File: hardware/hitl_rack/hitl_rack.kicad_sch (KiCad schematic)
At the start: 14 parts, among them J1 KH-1.27PH180-2X5P-L7.2-SMT, SW1 TS-1187A-B-A-B, U1 BlackPill

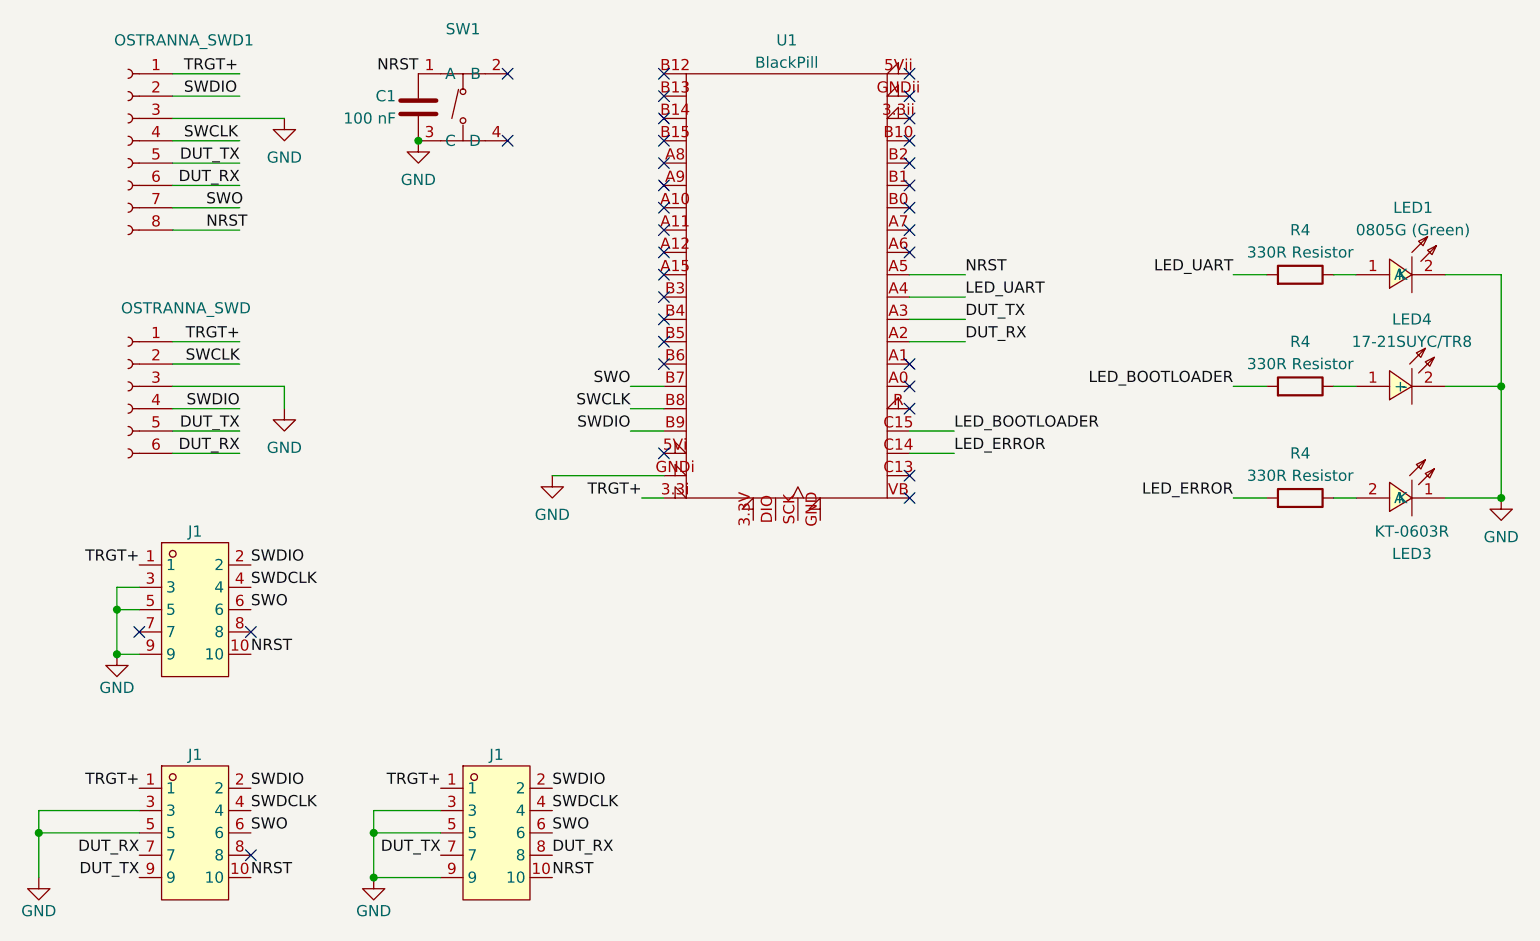
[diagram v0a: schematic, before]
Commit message: Finalize HITL rack PCB design and send to production
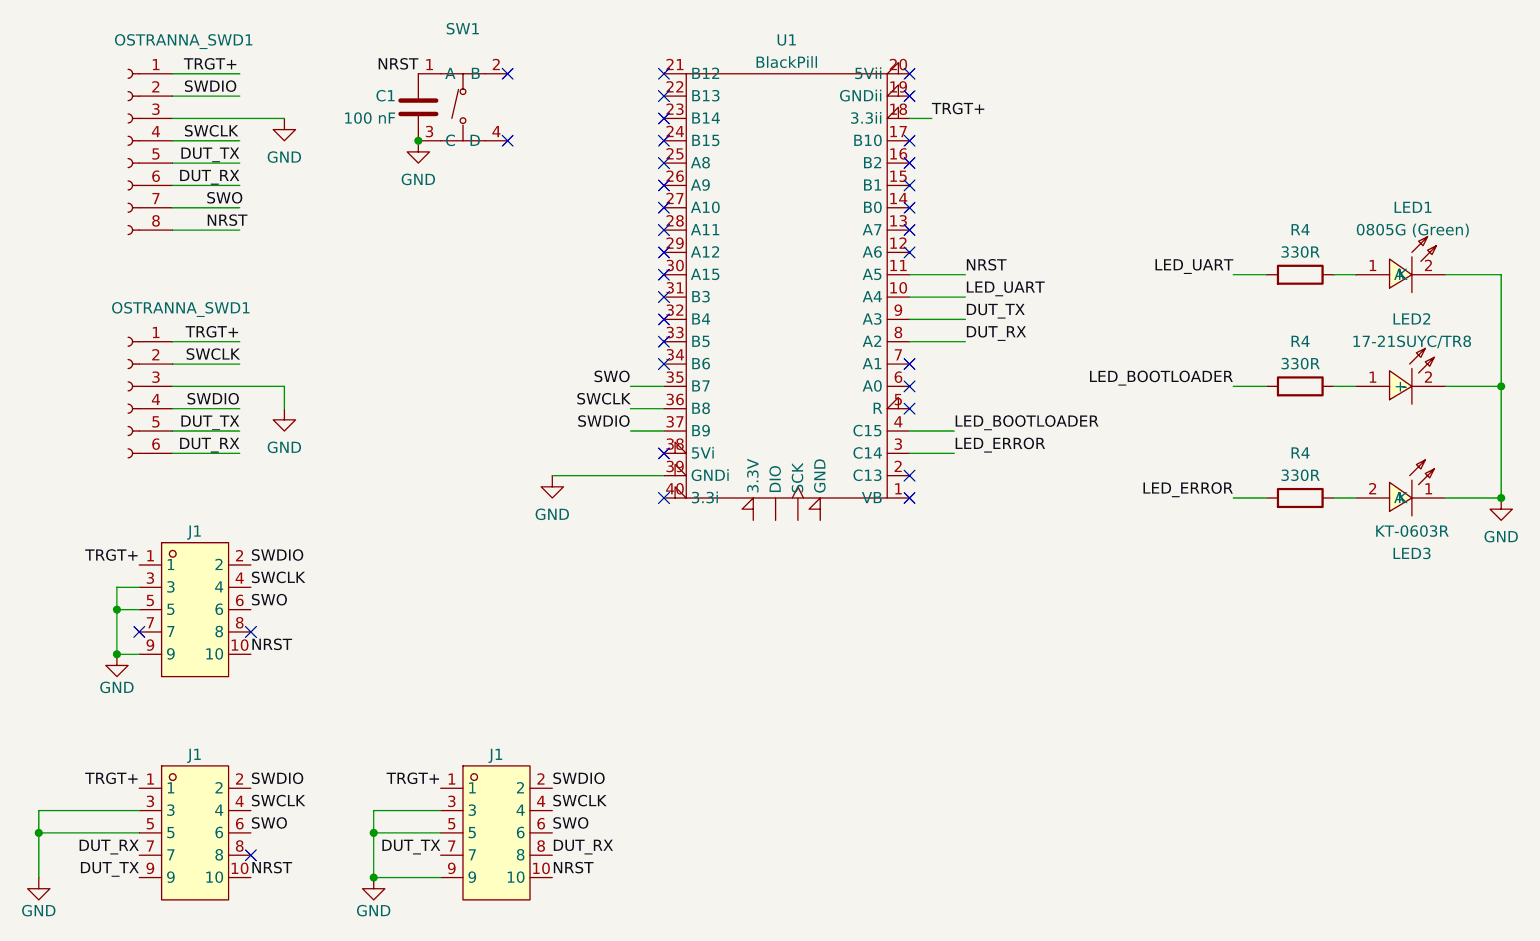
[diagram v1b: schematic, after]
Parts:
- R4: value 330R Resistor -> 330R
- renumbered LED4 to LED2, OSTRANNA_SWD to OSTRANNA_SWD1
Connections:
- net SWDCLK is gone; now on net SWCLK: J1.4, J1.4, J1.4
- net DUT_RX: now also U1.8 (A2); no longer U1.A2
- net DUT_TX: now also U1.9 (A3); no longer U1.A3
- net GND: now also U1.39 (GNDi); no longer U1.GNDi
- net LED_BOOTLOADER: now also U1.4 (C15); no longer U1.C15
- net LED_ERROR: now also U1.3 (C14); no longer U1.C14
- net LED_UART: now also U1.10 (A4); no longer U1.A4
- net NRST: now also U1.11 (A5); no longer U1.A5
- net SWCLK: now also U1.36 (B8); no longer U1.B8
- net SWDIO: now also U1.37 (B9); no longer U1.B9
- net SWO: now also U1.35 (B7); no longer U1.B7
- net TRGT+: now also U1.18 (3.3ii); no longer U1.3.3i
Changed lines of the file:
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@@
   (no_connect (at 121.92 101.6))
   (no_connect (at 149.86 83.82))
+  (no_connect (at 121.92 124.46))
   (no_connect (at 121.92 119.38))
   (no_connect (at 121.92 83.82))
@@
   (no_connect (at 121.92 106.68))
   (no_connect (at 149.86 88.9))
-  (no_connect (at 149.86 81.28))
   (no_connect (at 74.93 165.1))
   (no_connect (at 121.92 96.52))
@@
     (stroke (width 0) (type default))
   )
-  (wire (pts (xy 119.38 124.46) (xy 121.92 124.46))
-    (stroke (width 0) (type default))
-  )
   (wire (pts (xy 66.04 86.36) (xy 73.66 86.36))
     (stroke (width 0) (type default))
@@
     (stroke (width 0) (type default))
   )
+  (wire (pts (xy 152.4 81.28) (xy 149.86 81.28))
+    (stroke (width 0) (type default))
+  )
   (wire (pts (xy 198.12 111.76) (xy 200.66 111.76))
     (stroke (width 0) (type default))
@@
     (stroke (width 0) (type default))
   )
-  (label "SWDCLK" (at 74.93 160.02 0) (fields_autoplaced)
+  (label "SWCLK" (at 74.93 160.02 0) (fields_autoplaced)
     (effects (font (size 1.27 1.27)) (justify left bottom))
   )
@@
     (effects (font (size 1.27 1.27)) (justify right bottom))
   )
+  (label "TRGT+" (at 152.4 81.28 0) (fields_autoplaced)
+    (effects (font (size 1.27 1.27)) (justify left bottom))
+  )
   (label "LED_UART" (at 156.21 101.6 0) (fields_autoplaced)
     (effects (font (size 1.27 1.27)) (justify left bottom))
@@
     (effects (font (size 1.27 1.27)) (justify right bottom))
   )
-  (label "SWDCLK" (at 74.93 134.62 0) (fields_autoplaced)
-    (effects (font (size 1.27 1.27)) (justify left bottom))
-  )
-  (label "SWDCLK" (at 109.22 160.02 0) (fields_autoplaced)
+  (label "SWCLK" (at 74.93 134.62 0) (fields_autoplaced)
+    (effects (font (size 1.27 1.27)) (justify left bottom))
+  )
+  (label "SWCLK" (at 109.22 160.02 0) (fields_autoplaced)
     (effects (font (size 1.27 1.27)) (justify left bottom))
   )
@@
   )
   (label "DUT_TX" (at 96.52 165.1 180) (fields_autoplaced)
-    (effects (font (size 1.27 1.27)) (justify right bottom))
-  )
-  (label "TRGT+" (at 119.38 124.46 180) (fields_autoplaced)
     (effects (font (size 1.27 1.27)) (justify right bottom))
   )
@@
       (effects (font (size 1.27 1.27)))
     )
-    (property "Value" "330R Resistor" (at 194.31 121.92 90)
+    (property "Value" "330R" (at 194.31 121.92 90)
       (effects (font (size 1.27 1.27)))
     )
@@
   (symbol (lib_id "easyeda2kicad:17-21SUYC_TR8") (at 205.74 111.76 0) (mirror y) (unit 1)
     (in_bom yes) (on_board yes) (dnp no) (fields_autoplaced)
-    (property "Reference" "LED4" (at 207.01 104.14 0)
+    (property "Reference" "LED2" (at 207.01 104.14 0)
       (effects (font (size 1.27 1.27)))
     )
@@
       (project "hitl_rack"
         (path "/f0c86ddf-9c86-49a8-ba85-db01cb1dc88e"
-          (reference "LED4") (unit 1)
+          (reference "LED2") (unit 1)
         )
       )
@@
       (project "hitl_rack"
         (path "/f0c86ddf-9c86-49a8-ba85-db01cb1dc88e"
-          (reference "MANUAL_RESET") (unit 1)
+          (reference "MANUAL_RESET1") (unit 1)
         )
       )
@@
       (effects (font (size 1.27 1.27)))
     )
-    (property "Value" "330R Resistor" (at 194.31 96.52 90)
+    (property "Value" "330R" (at 194.31 96.52 90)
       (effects (font (size 1.27 1.27)))
     )
@@
       (project "hitl_rack"
         (path "/f0c86ddf-9c86-49a8-ba85-db01cb1dc88e"
-          (reference "ARM_CORTEX_CANONICAL") (unit 1)
+          (reference "ARM_CORTEX_CANONICAL1") (unit 1)
         )
       )
@@
       (effects (font (size 1.27 1.27)))
     )
-    (property "Value" "330R Resistor" (at 194.31 109.22 90)
+    (property "Value" "330R" (at 194.31 109.22 90)
       (effects (font (size 1.27 1.27)))
     )
@@
       (project "hitl_rack"
         (path "/f0c86ddf-9c86-49a8-ba85-db01cb1dc88e"
-          (reference "BLACK_MAGIC_UNIFIED") (unit 1)
+          (reference "BLACK_MAGIC_UNIFIED1") (unit 1)
         )
       )
@@
   (symbol (lib_id "Connector:Conn_01x06_Socket") (at 60.96 111.76 0) (mirror y) (unit 1)
     (in_bom yes) (on_board yes) (dnp no)
-    (property "Reference" "OSTRANNA_SWD" (at 74.93 102.87 0)
+    (property "Reference" "OSTRANNA_SWD1" (at 74.93 102.87 0)
       (effects (font (size 1.27 1.27)) (justify left))
     )
@@
       (project "hitl_rack"
         (path "/f0c86ddf-9c86-49a8-ba85-db01cb1dc88e"
-          (reference "OSTRANNA_SWD") (unit 1)
+          (reference "OSTRANNA_SWD1") (unit 1)
         )
       )
@@
       (project "hitl_rack"
         (path "/f0c86ddf-9c86-49a8-ba85-db01cb1dc88e"
-          (reference "ARM_CORTEX_EXTENDED") (unit 1)
+          (reference "ARM_CORTEX_EXTENDED1") (unit 1)
         )
       )
@@
       (project "hitl_rack"
         (path "/f0c86ddf-9c86-49a8-ba85-db01cb1dc88e"
-          (reference "FIREFLY_SWD") (unit 1)
+          (reference "FIREFLY_SWD1") (unit 1)
         )
       )
@@
       (effects (font (size 1.27 1.27)) hide)
     )
-    (pin "3.3V")
-    (pin "3.3i")
-    (pin "3.3ii")
-    (pin "5Vi")
-    (pin "5Vii")
-    (pin "A0")
-    (pin "A1")
-    (pin "A10")
-    (pin "A11")
-    (pin "A12")
-    (pin "A15")
-    (pin "A2")
-    (pin "A3")
-    (pin "A4")
-    (pin "A5")
-    (pin "A6")
-    (pin "A7")
-    (pin "A8")
-    (pin "A9")
-    (pin "B0")
-    (pin "B1")
-    (pin "B10")
-    (pin "B12")
-    (pin "B13")
-    (pin "B14")
-    (pin "B15")
-    (pin "B2")
-    (pin "B3")
-    (pin "B4")
-    (pin "B5")
-    (pin "B6")
-    (pin "B7")
-    (pin "B8")
-    (pin "B9")
-    (pin "C13")
-    (pin "C14")
-    (pin "C15")
-    (pin "DIO")
-    (pin "GND")
-    (pin "GNDi")
-    (pin "GNDii")
-    (pin "R")
-    (pin "SCK")
-    (pin "VB")
-    (instances
-      (project "hitl_rack"
+    (pin "")
+    (pin "")
+    (pin "")
+    (pin "")
+    (pin "1")
+    (pin "10")
+    (pin "11")
+    (pin "12")
+    (pin "13")
+    (pin "14")
+    (pin "15")
+    (pin "16")
+    (pin "17")
+    (pin "18")
+    (pin "19")
+    (pin "2")
+    (pin "20")
+    (pin "21")
+    (pin "22")
+    (pin "23")
+    (pin "24")
+    (pin "25")
+    (pin "26")
+    (pin "27")
+    (pin "28")
+    (pin "29")
+    (pin "3")
+    (pin "30")
+    (pin "31")
+    (pin "32")
+    (pin "33")
+    (pin "34")
+    (pin "35")
+    (pin "36")
+    (pin "37")
+    (pin "38")
+    (pin "39")
+    (pin "4")
+    (pin "40")
+    (pin "5")
+    (pin "6")
+    (pin "7")
+    (pin "8")
+    (pin "9")
+    (instances
+      (project "hitl_rack"
